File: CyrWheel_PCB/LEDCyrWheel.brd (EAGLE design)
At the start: 69 x 26.2 mm, 15 parts

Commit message: PCB design work
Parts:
- removed JP4_LED_STRIP_1, JP5_LED_STRIP_2: M01SMDNS, SparkFun:1X01NS
- removed U$4: ADAFRUIT_CC3000_WIFI, LEDCyrWheel:ADAFRUIT_CC3000_WIFI
- added IC1: 74LS125N, adafruit:DIL14
- added LED_CLK, LED_DATA: M01SMDNS, SparkFun:1X01NS
- added U$7: ADAFRUIT_BLE_FRIEND_SPI, LEDCyrWheel:ADAFRUIT_BLE_FRIEND_SPI
- moved BUTTON_2 63.3 mm to (11.0, 80.2)
- moved BUTTON_1 60.0 mm to (13.8, 80.2)
- moved U$6 1.27 mm to (19.3, 77.4), turned to 270 degrees
- moved R3 0.97 mm to (47.8, 76.0)
- moved R2 0.76 mm to (35.0, 75.9)
- moved R1 0.76 mm to (34.9, 78.6)
- moved R4 0.69 mm to (47.7, 78.7)
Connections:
- removed net 3V3: U$4.3_3V
- removed net N$3: U$1.15/A1, U$1.16/A2
- removed net N$4: U$1.12, U$2.MISO, U$4.MISO
- removed net N$5: U$1.13, U$2.SCLK, U$4.CLK
- removed net WIFI_CS: U$1.7, U$4.CS
- removed net WIFI_IRQ: U$1.5, U$4.IRQ
- removed net WIFI_VBEN: U$1.6, U$4.VBEN
- new net BT_CS: U$1.6, U$7.CS
- new net BT_IRQ: U$1.5, U$7.IRQ
- new net BT_RESET: U$1.4, U$7.RST
- new net LED_CLK: IC1.5, U$1.14/A0
- new net LED_DATA: IC1.2, U$1.7
- new net MISO: U$1.12, U$2.MISO, U$7.MISO
- new net MOSI: U$1.11, U$2.MOSI, U$7.MOSI
- new net SCK: U$1.13, U$2.SCLK, U$7.SCK
- net GND: now also IC1.1, IC1.4, IC1.7, U$7.GND; no longer U$4.GND
- net N$2: now also IC1.6, LED_CLK.1; no longer U$1.11, U$2.MOSI, U$4.MOSI
- net N_PIN_2_LED_STRIP: now also IC1.3, LED_DATA.1; no longer JP4_LED_STRIP_1.1, JP5_LED_STRIP_2.1, U$1.2
- net VIN: now also IC1.14, U$7.VIN; no longer U$4.VIN
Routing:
- net GND: track 166.3 -> 20.2 mm, vias 2 -> 4
- net VIN: track 124.8 -> 26.7 mm
- net BT_RESET: track 0.00 -> 88.0 mm, vias 0 -> 2
- net BT_IRQ: track 0.00 -> 82.3 mm, vias 0 -> 1
- net BT_CS: track 0.00 -> 77.1 mm, vias 0 -> 1
- net MISO: track 0.00 -> 60.0 mm, vias 0 -> 1
- net LED_DATA: track 0.00 -> 59.6 mm, vias 0 -> 1
- net SCK: track 0.00 -> 55.8 mm
- net MOSI: track 0.00 -> 52.4 mm, vias 0 -> 2
- net N_PIN_2_LED_STRIP: track 68.0 -> 17.2 mm, vias 1 -> 0
- net WIFI_IRQ: track 45.7 -> 0.00 mm
- net N$4: track 44.4 -> 0.00 mm
- net WIFI_VBEN: track 44.3 -> 0.00 mm
- net LED_CLK: track 0.00 -> 43.3 mm, vias 0 -> 2
- net WIFI_CS: track 41.4 -> 0.00 mm
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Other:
- board size 69 x 26.2 mm -> 80.4 x 26.2 mm
- board text added: "CLK"
- board text added: "DATA"
- board text added: "LED"
- board text removed: "LEDs"

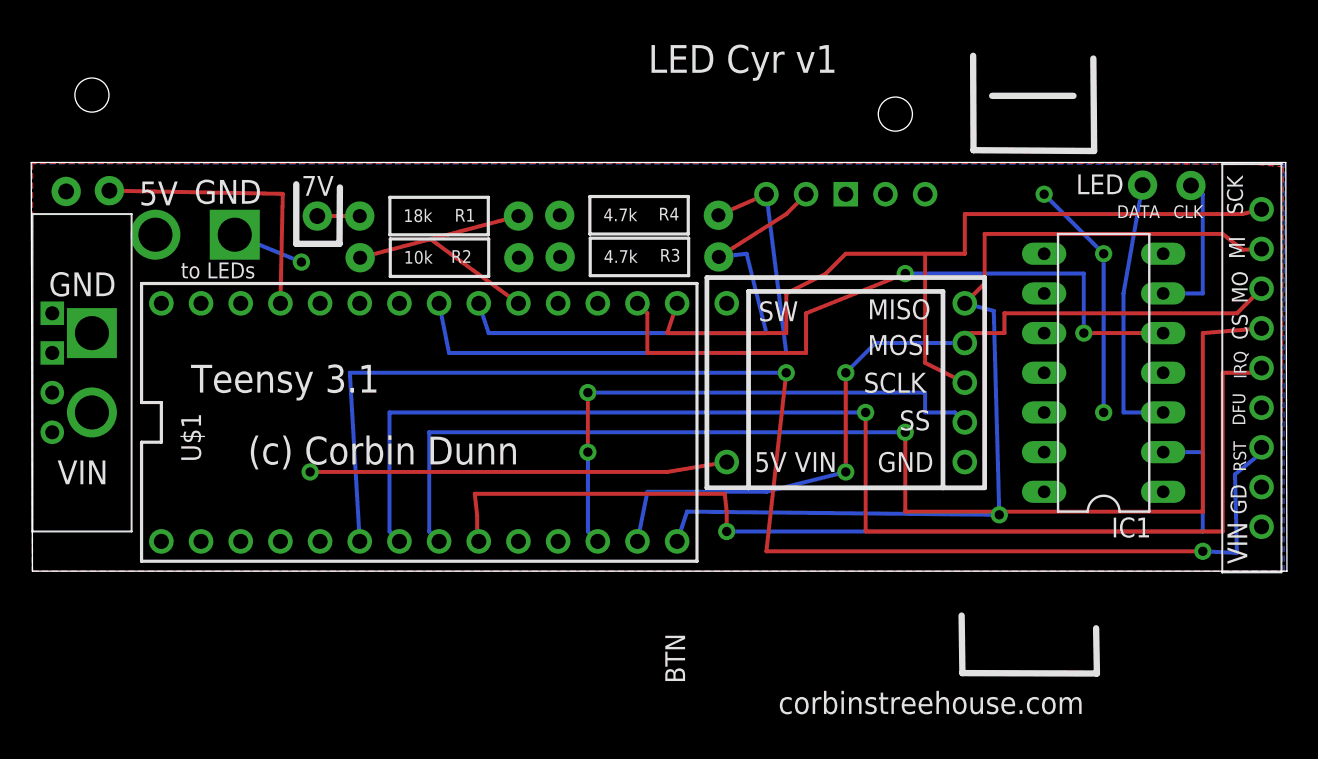
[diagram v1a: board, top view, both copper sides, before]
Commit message: Updated PCB design for new leds
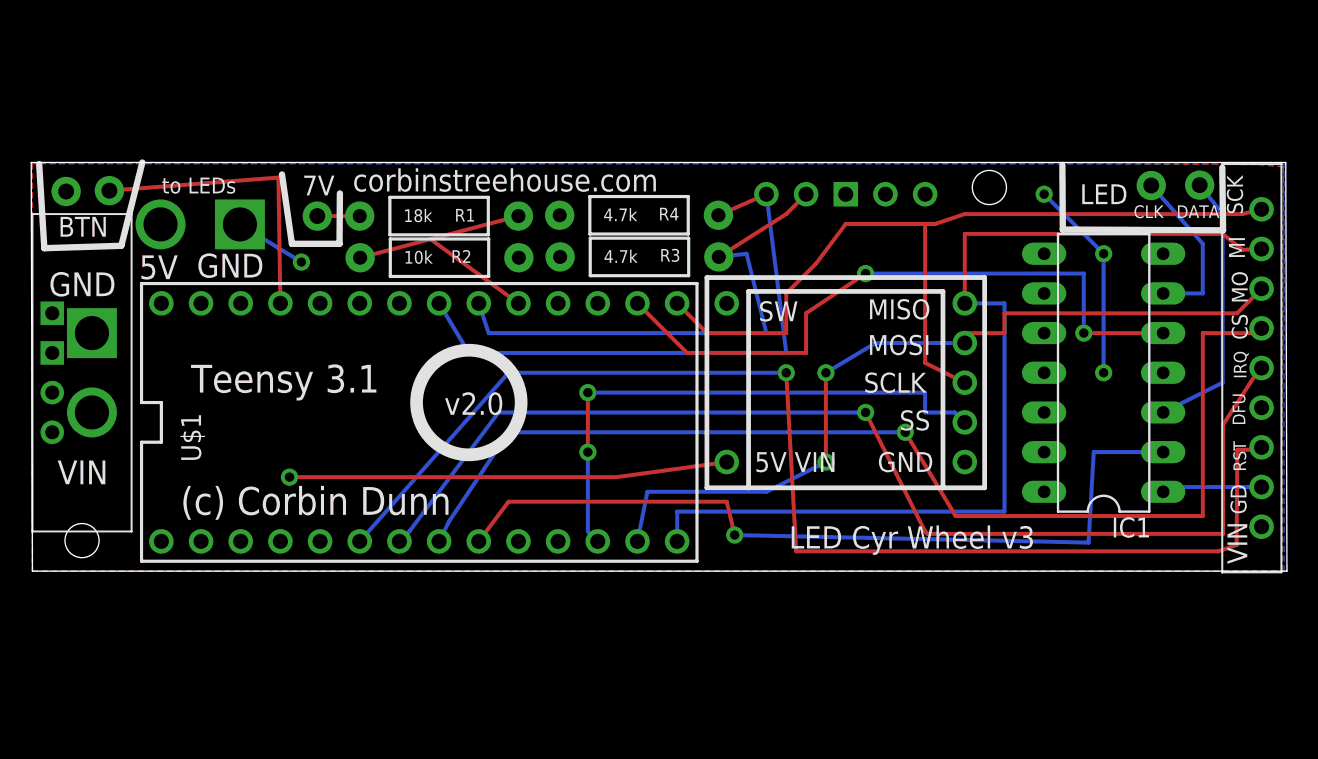
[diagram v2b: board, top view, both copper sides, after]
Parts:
- moved LED_DATA 3.66 mm to (83.6, 80.6)
- moved LED_CLK 2.54 mm to (80.5, 80.6)
- moved U$6 0.74 mm to (19.6, 78.1)
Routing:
- net BT_IRQ: track 82.3 -> 73.0 mm
- net BT_RESET: track 88.0 -> 79.6 mm, vias 2 -> 1
- net LED_DATA: track 59.6 -> 52.2 mm
- net BT_CS: track 77.1 -> 71.5 mm
- net GND: track 20.2 -> 24.1 mm
- net MISO: track 60.0 -> 62.5 mm, vias 1 -> 0
- net VIN: track 26.7 -> 28.1 mm
- net LED_CLK: track 43.3 -> 42.1 mm
- net SCK: track 55.8 -> 54.7 mm
- net N$2: track 9.83 -> 10.7 mm
- net N$7: track 38.4 -> 37.6 mm
- net N$8: track 18.1 -> 18.9 mm
- net MOSI: track 52.4 -> 51.8 mm
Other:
- board text added: "LED Cyr Wheel v3"
- board text added: "v2.0"
- board text removed: "LED Cyr v1"

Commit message: Updated PCB
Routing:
- net MISO: track 62.5 -> 61.4 mm
- net N$8: track 18.9 -> 19.7 mm
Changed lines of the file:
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@@
 <wire x1="87.5792" y1="76.5048" x2="86.36" y2="76.454" width="0.254" layer="1"/>
 <wire x1="86.36" y1="76.454" x2="85.09" y2="77.47" width="0.254" layer="1"/>
-<wire x1="85.09" y1="77.47" x2="68.58" y2="77.47" width="0.254" layer="1"/>
-<wire x1="68.58" y1="73.025" x2="68.58" y2="77.47" width="0.254" layer="1"/>
+<wire x1="85.09" y1="77.47" x2="69.85" y2="77.47" width="0.254" layer="1"/>
+<wire x1="68.58" y1="73.025" x2="69.85" y2="77.47" width="0.254" layer="1"/>
 <wire x1="50.165" y1="57.785" x2="50.165" y2="59.69" width="0.254" layer="16"/>
 <wire x1="50.165" y1="59.69" x2="71.12" y2="59.69" width="0.254" layer="16"/>
@@
 <wire x1="52.07" y1="71.12" x2="57.15" y2="71.12" width="0.254" layer="1"/>
 <wire x1="87.5792" y1="79.0448" x2="86.36" y2="78.74" width="0.254" layer="1"/>
-<wire x1="86.36" y1="78.74" x2="68.58" y2="78.74" width="0.254" layer="1"/>
-<wire x1="68.58" y1="78.74" x2="66.675" y2="78.105" width="0.254" layer="1"/>
+<wire x1="86.36" y1="78.74" x2="69.215" y2="78.74" width="0.254" layer="1"/>
+<wire x1="69.215" y1="78.74" x2="66.675" y2="78.105" width="0.254" layer="1"/>
 <wire x1="66.675" y1="78.105" x2="66.04" y2="78.105" width="0.254" layer="1"/>
 <wire x1="66.04" y1="78.105" x2="60.96" y2="78.105" width="0.254" layer="1"/>
@@
 <contactref element="U$1" pad="23/A9"/>
 <contactref element="BUTTON_1" pad="1"/>
-<wire x1="13.8176" y1="80.2386" x2="24.638" y2="81.0768" width="0.254" layer="1"/>
+<wire x1="13.8176" y1="80.2386" x2="13.7922" y2="80.2386" width="0.254" layer="1"/>
+<wire x1="13.7922" y1="80.2386" x2="13.7922" y2="81.026" width="0.254" layer="1"/>
+<wire x1="13.7922" y1="81.026" x2="24.638" y2="81.0768" width="0.254" layer="1"/>
 <wire x1="24.638" y1="81.0768" x2="24.765" y2="73.025" width="0.254" layer="1"/>
 </signal>

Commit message: PCB fixes
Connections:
- net N$6 renamed SDA
- net N$7 renamed SCL
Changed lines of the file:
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@@
 <text x="81.3054" y="79.2988" size="0.8128" layer="21" rot="R180">CLK</text>
 <text x="84.8868" y="79.2988" size="0.8128" layer="21" rot="R180">DATA</text>
-<hole x="70.1548" y="80.4418" drill="2.1844"/>
 <text x="57.3278" y="57.3278" size="1.4224" layer="21">LED Cyr Wheel v3</text>
 <text x="35.2552" y="65.8876" size="1.4224" layer="21">v2.0</text>
@@
 <wire x1="87.5792" y1="61.2648" x2="81.5848" y2="61.2648" width="0.254" layer="16"/>
 <wire x1="81.5848" y1="61.2648" x2="81.28" y2="60.96" width="0.254" layer="16"/>
-<wire x1="73.66" y1="80.01" x2="60.96" y2="80.01" width="0" layer="19" extent="1-1"/>
 </signal>
 <signal name="VIN">
@@
 <wire x1="66.04" y1="69.215" x2="66.04" y2="78.105" width="0.254" layer="1"/>
 </signal>
-<signal name="N$6">
+<signal name="SDA">
 <contactref element="R3" pad="P$2"/>
 <contactref element="U$3" pad="SDA"/>
@@
 <wire x1="54.61" y1="76.2" x2="52.832" y2="75.9968" width="0.254" layer="16"/>
 </signal>
-<signal name="N$7">
+<signal name="SCL">
 <contactref element="R4" pad="P$2"/>
 <contactref element="U$3" pad="SCL"/>
